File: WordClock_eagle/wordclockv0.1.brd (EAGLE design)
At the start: 63.2 x 57.1 mm, 39 parts, among them IC1 TLC5925, Q1 8MHz, Q2 32.768kHz, U1 MBT3906DW1T1G, U2 MBT3906DW1T1G, U3 MBT3906DW1T1G, U4 MBT3906DW1T1G, U5 MBT3906DW1T1G

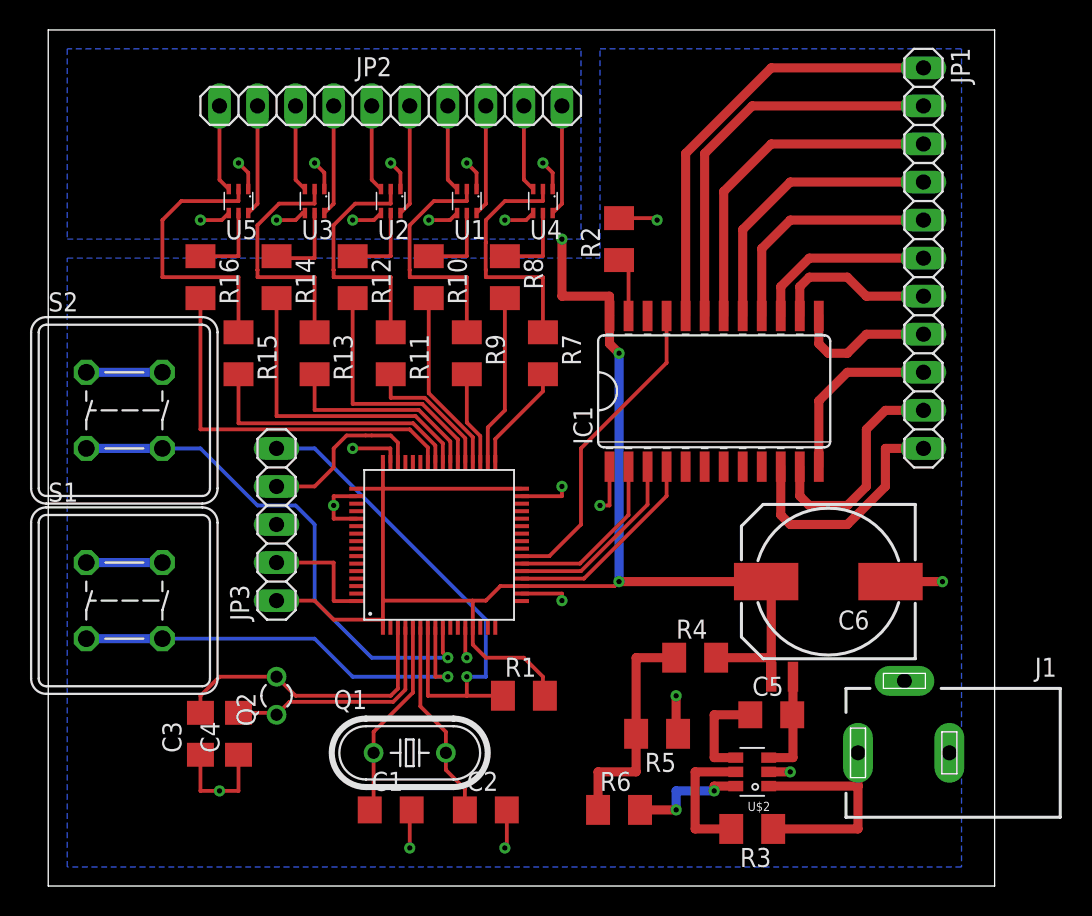
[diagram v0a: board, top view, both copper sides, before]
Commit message: Made a parts list from digikey. Changed some components bc cheaper
Whoa this was a piece of work.
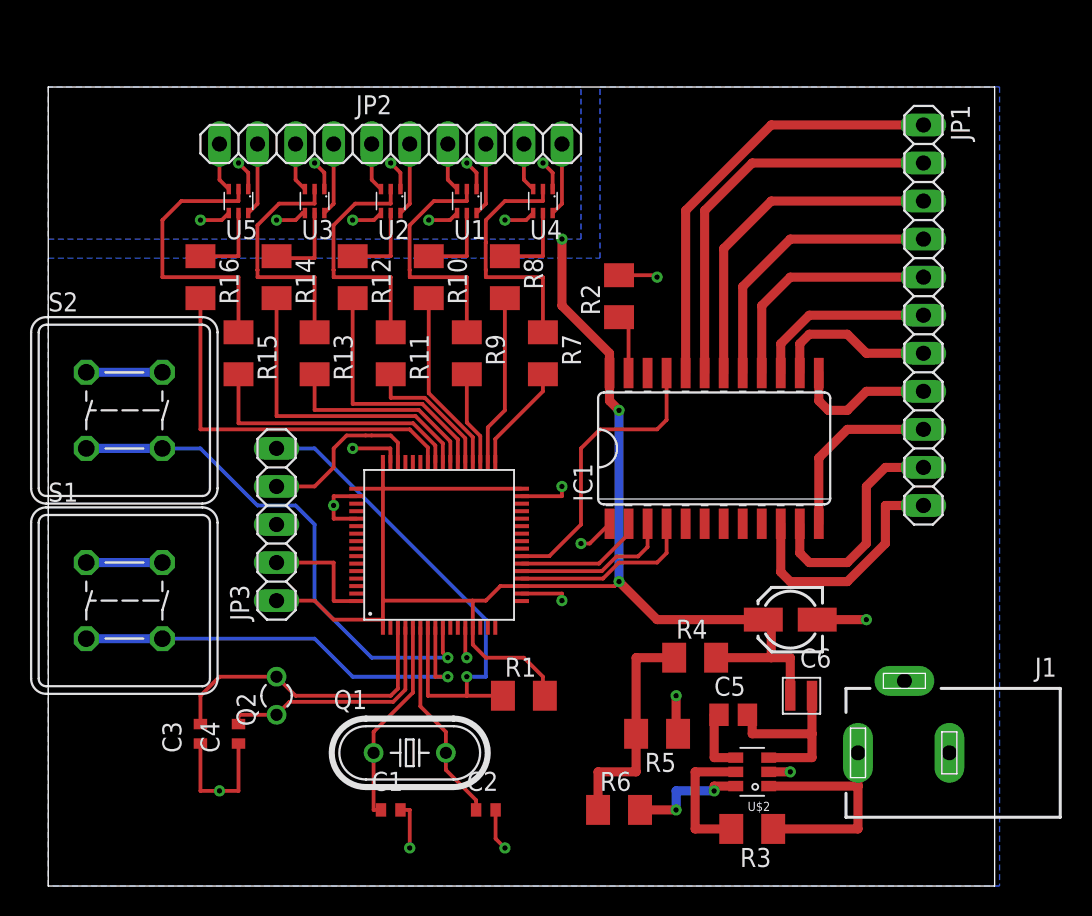
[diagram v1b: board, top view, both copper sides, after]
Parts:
- C1, C2, C3, C4: device rcl:C1206 -> rcl:C0402
- C5: value (none) -> 1uF; device rcl:C1206 -> rcl:C0805
- C6: device rcl:140CLH-1010 -> rcl:153CLV-0405
- R1: value 10k -> 100k
- moved IC1 3.81 mm to (44.5, 29.2)
- moved R2 3.81 mm to (38.1, 39.4)
- moved JP1 3.81 mm to (58.4, 38.1)
- moved C6 3.59 mm to (49.5, 17.8)
- moved C5 2.54 mm to (45.7, 11.4)
- moved JP2 2.54 mm to (22.9, 49.5)
- moved U$3 1.80 mm to (49.5, 12.7)
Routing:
- net N$10: track 7.09 -> 12.4 mm
- net SDI: track 11.7 -> 8.65 mm
- net COL6: track 5.81 -> 3.27 mm
- net COL10: track 5.81 -> 3.27 mm
- net COL9: track 7.41 -> 4.87 mm
- net COL8: track 5.81 -> 3.27 mm
- net COL7: track 7.41 -> 4.87 mm
- net COL5: track 7.41 -> 4.87 mm
- net COL4: track 5.81 -> 3.27 mm
- net COL3: track 7.41 -> 4.87 mm
- net COL2: track 5.81 -> 3.27 mm
- net COL1: track 7.41 -> 4.87 mm
- net CLK: track 12.8 -> 10.6 mm
- net N$6: track 6.71 -> 4.62 mm
- net !OE: track 21.1 -> 19.6 mm
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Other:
- board size 63.2 x 57.1 mm -> 63.2 x 53.3 mm

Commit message: Small changes to schematic and pcb
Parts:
- S1, S2: value DTE6K -> (none); device switch-misc:DTE6K -> switch-omron:B3F-10XX
- moved S2 5.68 mm to (7.62, 26.7)
- moved C3 4.02 mm to (11.4, 14.0), turned to 0 degrees
- moved S1 2.54 mm to (7.62, 19.1)
- moved C2 2.54 mm to (26.7, 5.08), turned to 180 degrees
- moved C4 1.80 mm to (11.4, 11.4), turned to 0 degrees
- moved C1 1.27 mm to (21.6, 5.08)
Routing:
- net N$4: track 20.4 -> 16.1 mm
- net N$20: track 35.1 -> 32.1 mm
- net N$16: track 29.3 -> 27.6 mm
- net GND: track 54.1 -> 54.8 mm, vias 13 -> 12
- net N$2: track 13.7 -> 13.2 mm

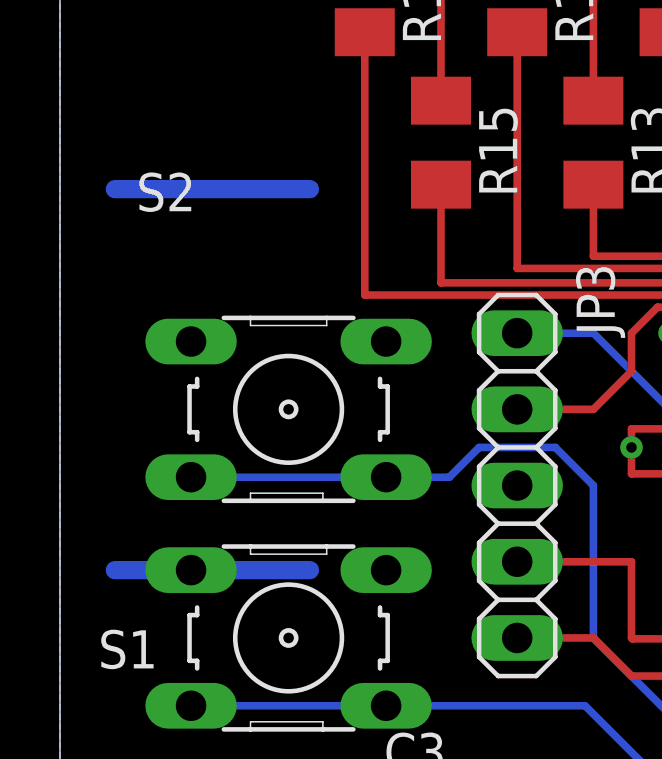
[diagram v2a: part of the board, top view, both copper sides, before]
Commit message: Removed wire stubs from board. Also added .cam file for generating jlcpcb
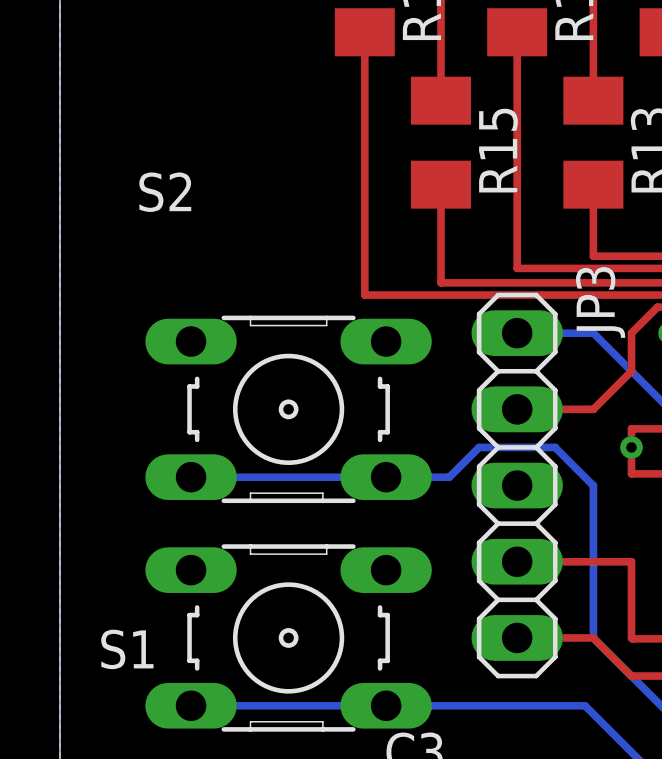
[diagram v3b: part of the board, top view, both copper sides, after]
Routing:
- net GND: track 54.8 -> 41.8 mm
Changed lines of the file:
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@@
 <?xml version="1.0" encoding="utf-8"?>
 <!DOCTYPE eagle SYSTEM "eagle.dtd">
-<eagle version="9.2.0">
+<eagle version="9.1.3">
 <drawing>
 <settings>
@@
 <contactref element="S2" pad="2"/>
 <contactref element="S1" pad="2"/>
-<wire x1="8.3312" y1="21.3106" x2="1.8288" y2="21.3106" width="0.6096" layer="16"/>
-<wire x1="8.3312" y1="34.0106" x2="1.8288" y2="34.0106" width="0.6096" layer="16"/>
 <contactref element="JP3" pad="3"/>
 <wire x1="37.465" y1="24.1808" x2="36.1442" y2="22.86" width="0.254" layer="1"/>

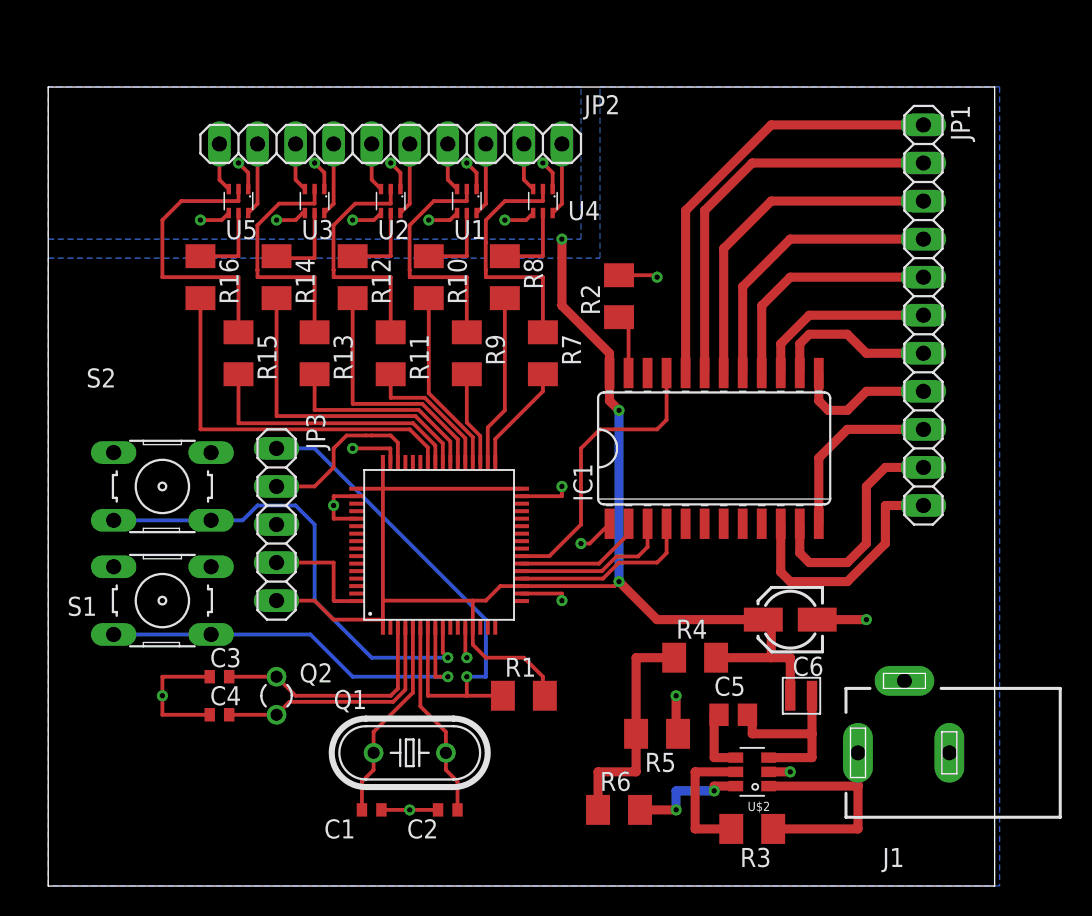
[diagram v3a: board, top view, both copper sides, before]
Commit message: Leds are now fed by VCC_RAW instead of 3V3
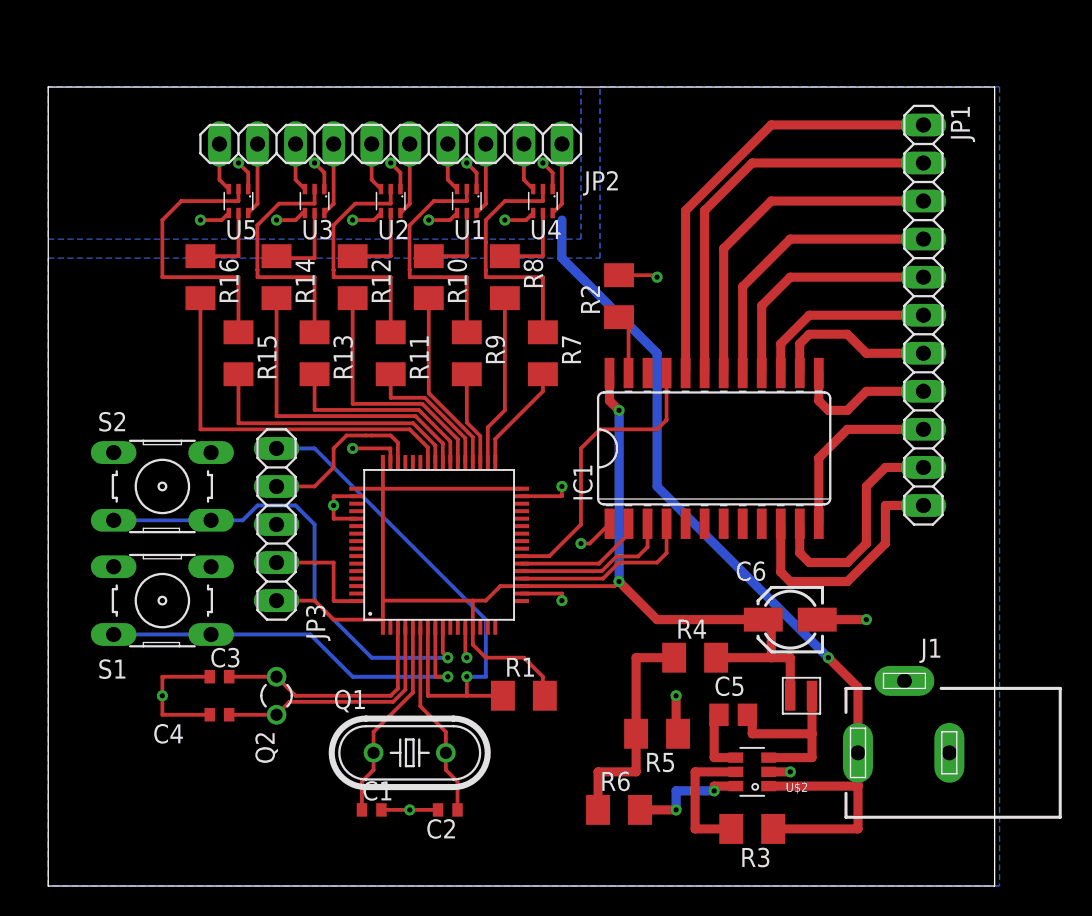
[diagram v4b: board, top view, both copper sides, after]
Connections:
- removed net N$5: J1.1, R3.1, U$2.P$1
- new net VCC_RAW: J1.1, R3.1, U$2.P$1, U1.1, U1.4, U2.1, U2.4, U3.1, U3.4, U4.1, U4.4, U5.1, U5.4
- net VDD: no longer U1.1, U1.4, U2.1, U2.4, U3.1, U3.4, U4.1, U4.4, U5.1, U5.4
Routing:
- net VCC_RAW: track 0.00 -> 80.9 mm, vias 0 -> 11
- net VDD: track 121.9 -> 91.2 mm, vias 13 -> 2
- net N$5: track 16.7 -> 0.00 mm
- added copper zone on layer 16, net VCC_RAW
- removed copper zone on layer 16, net VDD

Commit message: Updated the cam file for jlcpcb. The other files are just minor changes
idk bro seems pretty sketchy
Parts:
- JP1: device pinhead:1X11 -> pinhead:1X12
- moved JP1 1.27 mm to (58.4, 36.8)
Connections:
- removed net N$15: IC1.10, JP1.11
- removed net N$32: IC1.12, JP1.9
- removed net N$33: IC1.11, JP1.10
- new net OUT4: IC1.9, JP1.9
- new net OUT5: IC1.10, JP1.10
- new net OUT6: IC1.11, JP1.11
- new net OUT7: IC1.12, JP1.12
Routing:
- net N$15: track 16.6 -> 0.00 mm
- net OUT4: track 0.00 -> 16.0 mm
- net N$33: track 15.3 -> 0.00 mm
- net OUT5: track 0.00 -> 12.9 mm
- net N$32: track 12.2 -> 0.00 mm
- net OUT6: track 0.00 -> 10.9 mm
- net OUT7: track 0.00 -> 7.53 mm
- net GND: track 41.8 -> 39.2 mm
- net N$25: track 26.8 -> 24.5 mm
- net N$31: track 9.63 -> 7.49 mm
- net N$26: track 23.0 -> 21.5 mm
- net N$24: track 29.1 -> 27.6 mm
- net N$27: track 19.1 -> 18.4 mm
- net N$28: track 16.1 -> 15.3 mm

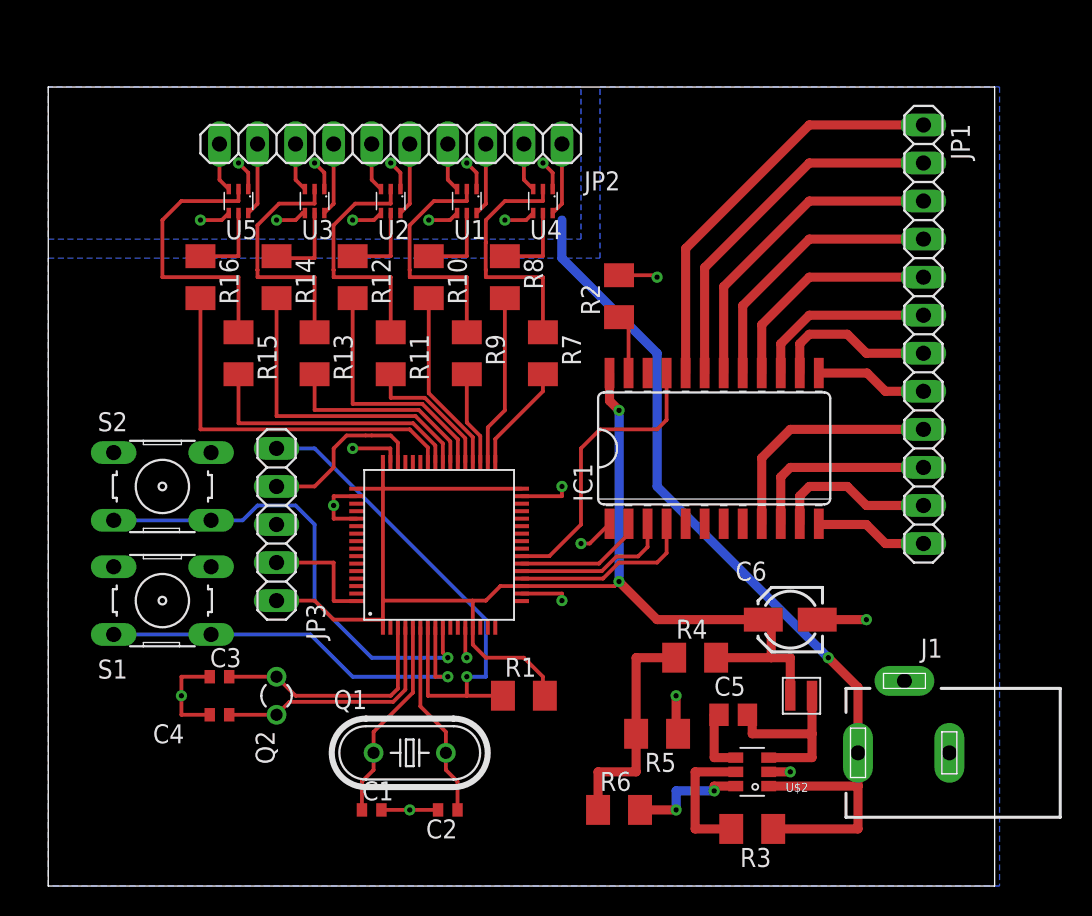
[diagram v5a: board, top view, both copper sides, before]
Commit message: Fixing huge error with stm32 pinout. Also revising board
My package was numbered differently than the diagram in the datasheet. Didn't realize until the thing was hot to the touch and not responding. sucks to be me
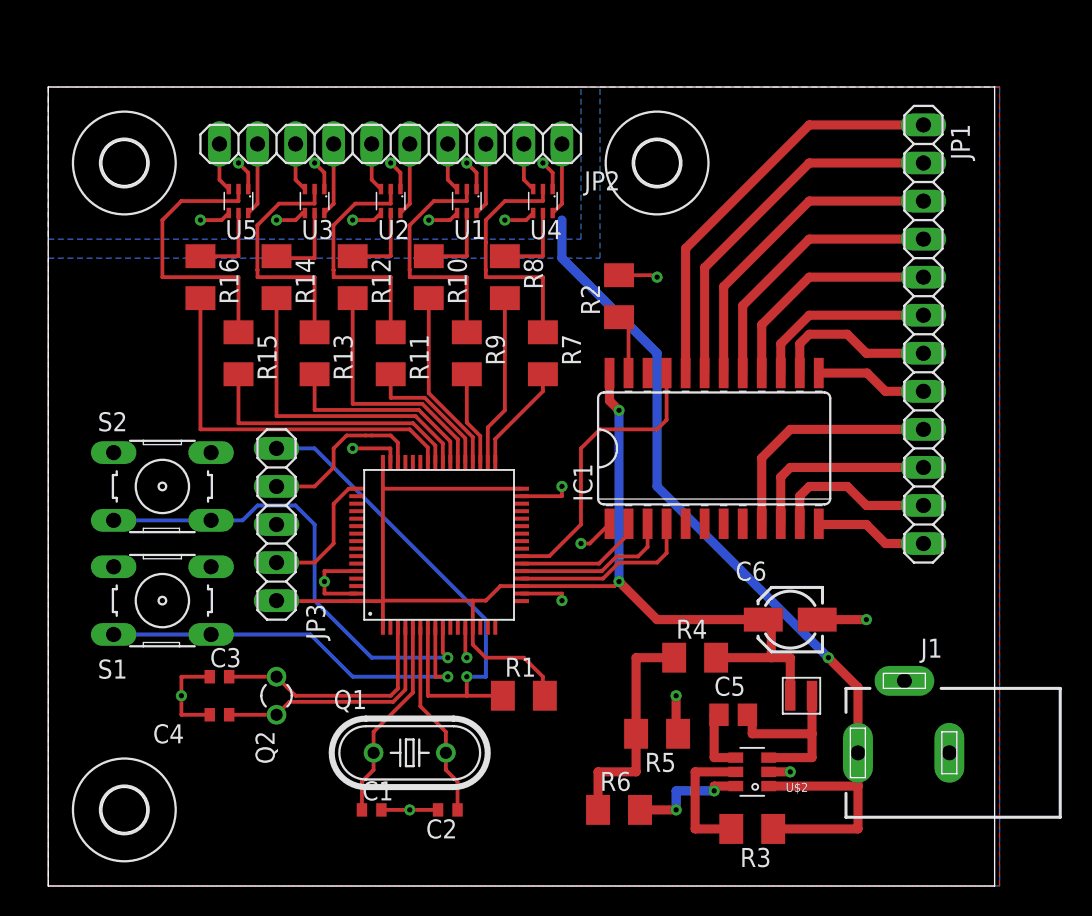
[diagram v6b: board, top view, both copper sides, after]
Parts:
- added U$4, U$5, U$6: (no value), holes:3,0
- U$1: value STM32F030RCT6TR -> STM32F030RCT6TRLQFP64
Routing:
- net VDD: track 91.2 -> 88.9 mm
- net GND: track 39.2 -> 40.5 mm
- net SWDCLK: track 7.90 -> 8.94 mm
- added copper zone on layer 1, net GND
